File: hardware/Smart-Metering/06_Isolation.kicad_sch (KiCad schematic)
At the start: 0 parts

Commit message: Implementa folha de isolação logo após o ADE9430
06_Isolation define a barreira reforçada entre o domínio metrológico
(potencial da rede, GND = neutro) e o domínio seguro (GND_SYS):

- U601 ISO7741: SCLK, MOSI, SS para o ADE9430; MISO de volta;
- U602 ISO7742: RESET e SS_SID para o lado da rede; CF1/CF2 de volta;
- U603 ISO7740: IRQ0, IRQ1, DREADY e ZX de volta;
- pull-ups de 10 kΩ nas saídas do ADE9430 e 1 kΩ em série no RESET;
- U604 MCP3204 lê SID_A..SID_N de forma ratiométrica, compartilhando o
  SPI isolado com chip select próprio;
- PS601 DC/DC isolado reforçado (+5V -> +5V_ISO) e U605 LDO
  TPS7A2033 gerando +3V3_ADE.

Novos símbolos: ISO7740/7741/7742, MCP3204, DCDC_Isolated e
LDO_EN_SOT23-5 (pinouts a conferir nos datasheets).
ARCHITECTURE.md e README atualizados com a nova posição da barreira.

Co-Authored-By: Claude Opus 5.5 <noreply@anthropic.com>
Claude-Session: https://claude.ai/code/session_012B8cVkhtjf3eg98UdpNCpf
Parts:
- added C601, C602, C603, C604, C605, C606, C607, C613: 100nF, Capacitor_SMD:C_0603_1608Metric, symbol SmartMetering:C_Vert
- added C609, C610, C612: 10uF, Capacitor_SMD:C_0805_2012Metric, symbol SmartMetering:C_Vert
- added C611: 1uF, Capacitor_SMD:C_0603_1608Metric, symbol SmartMetering:C_Vert
- added PS601: 5V->5V 1W reinf., symbol SmartMetering:DCDC_Isolated
- added R601: 1k, Resistor_SMD:R_0603_1608Metric, symbol SmartMetering:R_Vert
- added R602, R603, R604, R605, R606, R607: 10k, Resistor_SMD:R_0603_1608Metric, symbol SmartMetering:R_Vert
- added U601: ISO7741, Package_SO:SOIC-16W_7.5x10.3mm_P1.27mm, symbol SmartMetering:ISO7741
- added U602: ISO7742, Package_SO:SOIC-16W_7.5x10.3mm_P1.27mm, symbol SmartMetering:ISO7742
- added U603: ISO7740, Package_SO:SOIC-16W_7.5x10.3mm_P1.27mm, symbol SmartMetering:ISO7740
- added U604: MCP3204, Package_SO:SOIC-14_3.9x8.7mm_P1.27mm, symbol SmartMetering:MCP3204
- added U605: TPS7A2033, Package_TO_SOT_SMD:SOT-23-5, symbol SmartMetering:LDO_EN_SOT23-5
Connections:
- new net +3V3: C602.1, C604.1, C606.1, U601.1 (VCC1), U601.7 (EN1), U602.10 (EN2), U602.16 (VCC2), U603.10 (EN2), U603.16 (VCC2)
- new net +3V3_ADE: C601.1, C603.1, C605.1, C607.1, C612.1, C613.1, R602.1, R603.1, R604.1, R605.1, R606.1, R607.1, U601.10 (EN2), U601.16 (VCC2), U602.1 (VCC1), U602.7 (EN1), U603.1 (VCC1), U604.13 (VREF), U604.14 (VDD), U605.5 (OUT)
- new net +5V: C609.1, PS601.1 (+VIN)
- new net +5V_ISO: C610.1, C611.1, PS601.3 (+VOUT), U605.1 (IN), U605.3 (EN)
- new net CF1_ADE: R606.2, U602.3 (INA)
- new net CF2_ADE: R607.2, U602.4 (INB)
- new net DREADY_ADE: R604.2, U603.5 (INC)
- new net GND: C601.2, C603.2, C605.2, C607.2, C610.2, C611.2, C612.2, C613.2, PS601.4 (-VOUT), U601.15 (GND2), U601.9 (GND2), U602.2 (GND1), U602.8 (GND1), U603.2 (GND1), U603.8 (GND1), U604.12 (AGND), U604.7 (DGND), U605.2 (GND)
- new net GND_SYS: C602.2, C604.2, C606.2, C609.2, PS601.2 (-VIN), U601.2 (GND1), U601.8 (GND1), U602.15 (GND2), U602.9 (GND2), U603.15 (GND2), U603.9 (GND2)
- new net IRQ0_ADE: R602.2, U603.3 (INA)
- new net IRQ1_ADE: R603.2, U603.4 (INB)
- new net MCU_CF1: U602.14 (OUTA)
- new net MCU_CF2: U602.13 (OUTB)
- new net MCU_DREADY: U603.12 (OUTC)
- new net MCU_IRQ0: U603.14 (OUTA)
- new net MCU_IRQ1: U603.13 (OUTB)
- new net MCU_MISO: U601.6 (OUTD)
- new net MCU_MOSI: U601.4 (INB)
- new net MCU_RESET_ADE: U602.12 (INC)
- new net MCU_SCLK: U601.3 (INA)
- new net MCU_SS_ADE: U601.5 (INC)
- new net MCU_SS_SID: U602.11 (IND)
- new net MCU_ZX: U603.11 (OUTD)
- new net MISO_ADE: U601.11 (IND), U604.10 (DOUT)
- new net MOSI_ADE: U601.13 (OUTB), U604.9 (DIN)
- new net RESET_ADE: R601.1
- new net RESET_DRV: R601.2, U602.5 (OUTC)
- new net SCLK_ADE: U601.14 (OUTA), U604.11 (CLK)
- new net SID_A: U604.1 (CH0)
- new net SID_B: U604.2 (CH1)
- new net SID_C: U604.3 (CH2)
- new net SID_N: U604.4 (CH3)
- new net SS_ADE: U601.12 (OUTC)
- new net SS_SID: U602.6 (OUTD), U604.8 (~{CS}/SHDN)
- new net ZX_ADE: R605.2, U603.6 (IND)
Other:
- note added: "ALIMENTAÇÃO ISOLADA +5V (domínio seguro, folha 09) -> PS601 DC/DC isolado reforçado -> +5V_ISO -> U605 LDO -> +3V3_ADE PS601: isolação reforçada >= 4 kVAC e tensão de trabalho >= 300 VAC (CAT III 300 V). Consumo estimado do lado da rede: ADE9430 + 3 isoladores (lado 1) + MCP3204 < 100 mA. LAYOUT: distância de escoamento >= 8 mm sob U601-U603 e PS601; nenhuma trilha ou plano atravessa a barreira. 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"
- note added: "IDENTIFICAÇÃO DOS SENSORES (U604 MCP3204) Mede SID_A..SID_N (pull-up 10 kΩ, folha 03) de forma ratiométrica: VREF = +3V3_ADE. Compartilha SCLK/MOSI/MISO com o ADE9430; chip select próprio (SS_SID). MCP3204 aceita SPI de no máximo ~1 MHz a 3,3 V: o MCU deve reduzir o clock ao acessá-lo. Conferir no datasheet do ADE9430 que MISO fica em alta impedância com SS em nível alto."
- note added: "ISOLAÇÃO DO DOMÍNIO METROLÓGICO Esquerda: domínio metrológico (ADE9430, sensores). GND = neutro -> potencial da rede. Direita: domínio seguro (MCU, ESP32-P4, USB, Ethernet, microSD). GND_SYS. Todo sinal entre os domínios passa por U601-U603 ou PS601."
- note added: "SINAIS ISOLADOS (ISO774x, reforçado 5 kVrms, SOIC-16 largo) U601 ISO7741: SCLK, MOSI, SS -> ADE9430; MISO <- (barramento compartilhado com U604) U602 ISO7742: RESET, SS_SID -> ; CF1, CF2 <- (pulsos de energia) U603 ISO7740: IRQ0, IRQ1, DREADY, ZX <- Saídas padrão em nível alto sem alimentação do lado de entrada: SS desativado, RESET solto. Pull-ups de 10 kΩ (R602-R607) nas saídas do ADE9430 que v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"
- company: (none) -> Smart-Metering
- title: (none) -> Isolation - Metrology Barrier

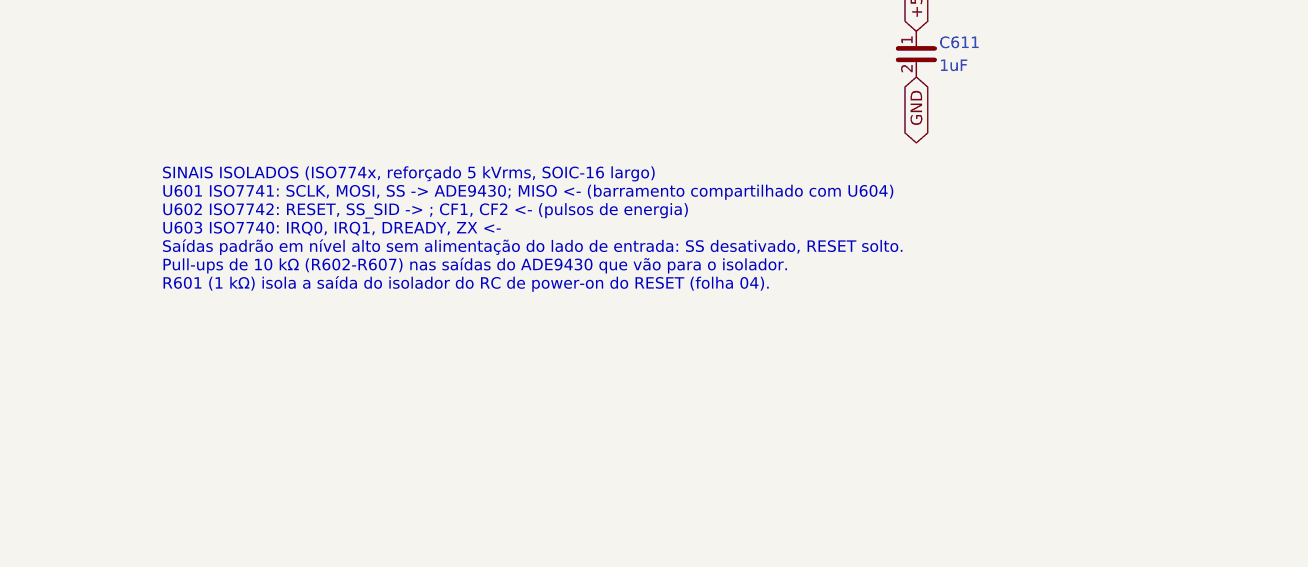
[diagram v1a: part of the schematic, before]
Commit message: Implementa folha de entrada de energia e numera referências por folha
01_Power_Input:
- modo padrão: LINE_A/B/C -> fusível -> diodo S1M em OU para o
  barramento HV, retorno no NEUTRAL via JP101; o instrumento segue
  alimentado com qualquer fase presente;
- modo auxiliar (J101, 100-240 VAC, com varistor): F104/D104/JP102,
  não montados por padrão; para rede 3 fios sem neutro;
- R101 fusível limita inrush, C101 4,7 uF/450 V no barramento;
- PS101 módulo AC/DC isolado 5 V / 2 A (ex.: IRM-10-5) gerando
  VIN_ACDC para a folha 09, referenciado a GND_SYS.

Referências renumeradas por folha para evitar colisões: folha 02 passa
a 2xx (R201 = ligação neutro/GND), folha 03 a 3xx e folha 04 a 4xx
(U401 = ADE9430).

Novos símbolos: D_Rect, CP_Vert, Jumper_2 e ACDC_Module.

Co-Authored-By: Claude Opus 5.5 <noreply@anthropic.com>
Claude-Session: https://claude.ai/code/session_012B8cVkhtjf3eg98UdpNCpf
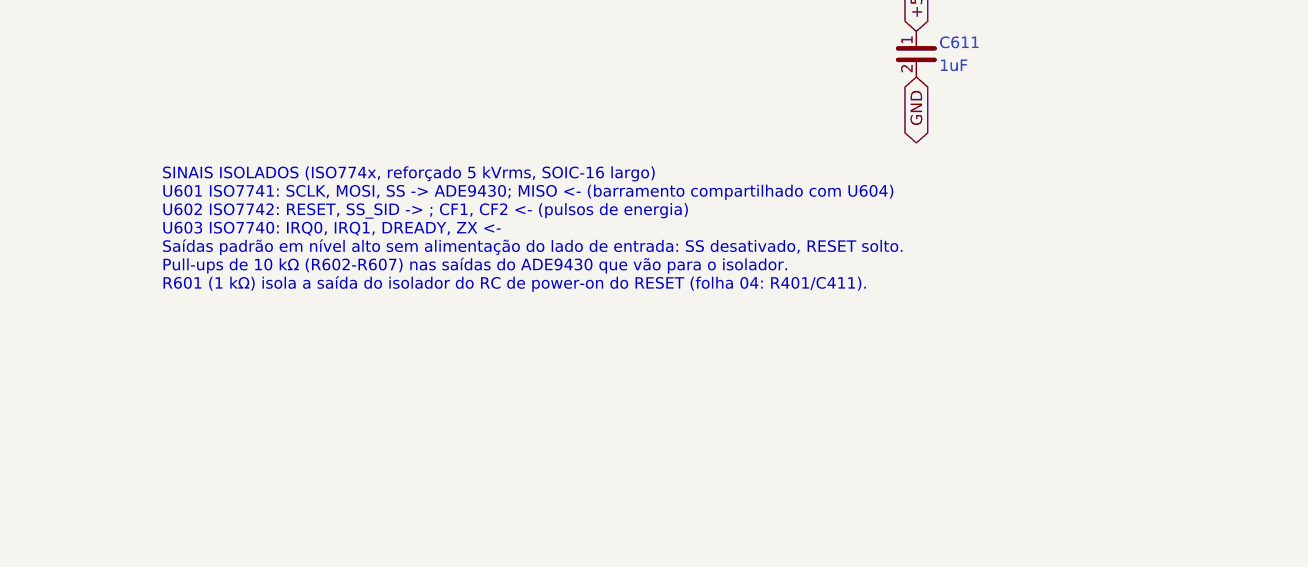
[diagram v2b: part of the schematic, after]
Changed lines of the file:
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@@
 		(effects (font (size 1.27 1.27)) (justify left top))
 	)
-	(text "SINAIS ISOLADOS (ISO774x, reforçado 5 kVrms, SOIC-16 largo)\nU601 ISO7741: SCLK, MOSI, SS -> ADE9430; MISO <- (barramento compartilhado com U604)\nU602 ISO7742: RESET, SS_SID -> ; CF1, CF2 <- (pulsos de energia)\nU603 ISO7740: IRQ0, IRQ1, DREADY, ZX <-\nSaídas padrão em nível alto sem alimentação do lado de entrada: SS desativado, RESET solto.\nPull-ups de 10 kΩ (R602-R607) nas saídas do ADE9430 que vão para o isolador.\nR601 (1 kΩ) isola a saída do isolador do RC de power-on do RESET (folha 04)."
+	(text "SINAIS ISOLADOS (ISO774x, reforçado 5 kVrms, SOIC-16 largo)\nU601 ISO7741: SCLK, MOSI, SS -> ADE9430; MISO <- (barramento compartilhado com U604)\nU602 ISO7742: RESET, SS_SID -> ; CF1, CF2 <- (pulsos de energia)\nU603 ISO7740: IRQ0, IRQ1, DREADY, ZX <-\nSaídas padrão em nível alto sem alimentação do lado de entrada: SS desativado, RESET solto.\nPull-ups de 10 kΩ (R602-R607) nas saídas do ADE9430 que vão para o isolador.\nR601 (1 kΩ) isola a saída do isolador do RC de power-on do RESET (folha 04: R401/C411)."
 		(exclude_from_sim no)(at 200.66 101.6 0)
 		(effects (font (size 1.27 1.27)) (justify left top))
